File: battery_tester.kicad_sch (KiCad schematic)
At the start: 76 parts, among them J1 Conn_BAL, J10 Conn_01x02_Pin, J2 Conn_BAT, J3 Screw_Terminal_01x02, J4 Screw_Terminal_01x02, J6 CON05, J7 CON05, J8 MicroSD_Connector_500901-0801, J9 Conn_01x02_Pin, M1 OLED12864-I2C, Q1 IRF8721PBF-1, U1 STM32G484RETx, U2 ACS713xLCTR-30A, U3 BTS7004-1EPP, U4 BTS7004-1EPP, U6 TMP101, X1 ASCO

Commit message: Almost finalize schematics
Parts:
- removed J?: USB_Micro-B_Rec, _Connectors_GRZ:USB_Micro-B_Molex_105017-0001, symbol _GRZ_Connectors:USB_Micro-B_Rec
- added C29: 100nF, Capacitor_SMD:C_0603_1608Metric, symbol Device:C
- added J11: USB-C_12pin, _Connectors_GRZ:USB-C_HRO_C-31-M-12, symbol _GRZ_Connectors:USB-C_12pin
- added J5: Conn_01x02_Pin, symbol Connector:Conn_01x02_Pin
- added PB6: KSC3J, _Switches_GRZ:KSC3J, symbol _GRZ_Switches:KSC3J
- added R27, R51: 40k, Resistor_SMD:R_0603_1608Metric, symbol Device:R
- added R41, R42: 5.1K, Resistor_SMD:R_0603_1608Metric, symbol Device:R
- added TP5 (x7): TestPoint, TestPoint:TestPoint_Pad_D2.0mm, symbol Connector:TestPoint
- added X2: ASAK, _Misc_GRZ:Osc_ASAK, symbol _GRZ_Misc:ASAK
- C27, C28, C_{BYP}1, C_{OUT}1, C_{OUT}2, C_{SENSE}1, C_{SENSE}2, C_{VS}1, C_{VS}2: footprint (none) -> Capacitor_SMD:C_0603_1608Metric
- D1, D2: footprint (none) -> LED_SMD:LED_0603_1608Metric
- J10, J9: footprint (none) -> Connector_PinHeader_2.54mm:PinHeader_1x02_P2.54mm_Vertical
- J3, J4: footprint (none) -> TerminalBlock:TerminalBlock_bornier-2_P5.08mm
- J8: footprint MicroSD_500901-0801 -> _Connectors_GRZ:MicroSD_500901-0801
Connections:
- net +24V: now also J5.1 (Pin_1)
- net +3.3V: now also X1.1 (TS), C29.1, PB6.1, PB6.4, X2.1 (TS), X2.4 (VDD)
- net BOOT0: now also PB6.2, PB6.3, R51.1
- net BTS1_SENSE: now also TP5.1
- net BTS2_SENSE: now also TP5.1
- net FAN: now also R27.1
- net GND: now also C29.2, J11.A1-B12 (GND), J11.B1-A12 (GND), J11.S (Shield), J5.2 (Pin_2), R27.2, R41.2, R42.2, R51.2, X2.2 (GND)
- net SD1ck: now also TP5.1
- net SD1cs: now also TP5.1
- net SD1di: now also TP5.1
- net SD1do: now also TP5.1
- net USB_DM: now also J11.A7 (D-1), J11.B7 (D-2)
- net USB_DP: now also J11.A6 (D+1), J11.B6 (D+2)
- net USB_VBUS: now also J11.A4-B9 (VBUS), J11.B4-A9 (VBUS)
- net V_{ACS}: now also TP5.1
- net VBAT: now reaches U1.1 (VBAT)
- net LSO: now reaches U1.3 (PC14)
- net LSO: now also X2.3 (OUT)
- new net: J11.B5 (CC2), R41.1
- new net: J11.A5 (CC1), R42.1
- no-connect marks 1 -> 11
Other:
- note added: "voltage divider 5V -> 3.3V"
- note removed: "TS ? -->"
- note removed: "usb detect !!! USB-C ???"
- note removed: "voltage divider 3.3V -> 5V"
- moved on the sheet: C1, C19, C20, C21, C22, C23, C24, J6, J7

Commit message: Finish layout.
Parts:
- removed J5: Conn_01x02_Pin, symbol Connector:Conn_01x02_Pin
- removed J8: MicroSD_Connector_500901-0801, _Connectors_GRZ:MicroSD_500901-0801, symbol _GRZ_Connectors:MicroSD_Connector_500901-0801
- added H1 (x4): MountingHole, _MountingHole_GRZ:MountingHole_3.2mm_M3, symbol Mechanical:MountingHole
- added J13: MicroSD_Connector_503182-1852, _Connectors_GRZ:MicroSD_503182-1852, symbol _GRZ_Connectors:MicroSD_Connector_503182-1852
- added J5: Conn_01x07_Pin, _Connectors_GRZ:PicoBlade_53398-0771, symbol Connector:Conn_01x07_Pin
- J1: footprint Connector_JST:JST_XH_B7B-XH-A_1x07_P2.50mm_Vertical -> Connector_JST:JST_XH_S7B-XH-A_1x07_P2.50mm_Horizontal
- J10, J9: footprint Connector_PinHeader_2.54mm:PinHeader_1x02_P2.54mm_Vertical -> Connector_PinHeader_2.54mm:PinHeader_1x02_P2.54mm_Horizontal
- TP5: footprint TestPoint:TestPoint_Pad_D2.0mm -> TestPoint:TestPoint_Pad_D1.0mm
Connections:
- net +24V: now also J10.1 (Pin_1), J9.1 (Pin_1); no longer J10.2 (Pin_2), J9.2 (Pin_2)
- net +3.3V: now also J13.4 (VDD), J5.2 (Pin_2)
- net BTS1_DEN: now also U1.22 (PC4); no longer U1.20 (PA6)
- net BTS1_SENSE: now also U1.20 (PA6); no longer U1.22 (PC4)
- net BTS2_DEN: now also U1.24 (PB0); no longer U1.25 (PB1)
- net BTS2_IN: now also U1.25 (PB1); no longer U1.24 (PB0)
- net GND: now also J1.1 (Pin_1), J13.6 (GND), J13.9 (SW1), J13.S (SHIELD), J5.1 (Pin_1); no longer J1.7 (Pin_7)
- net LED_HB: now also U1.53 (PC11); no longer U1.54 (PC12)
- net LED_RUN: now also U1.52 (PC10); no longer U1.53 (PC11)
- net NFC_CLK: now also J5.6 (Pin_6)
- net NFC_IRQ: now also J5.7 (Pin_7)
- net NFC_MISO: now also J5.5 (Pin_5)
- net NFC_MOSI: now also J5.4 (Pin_4)
- net NFC_SS: now also J5.3 (Pin_3)
- net POWER_KEY: now also U1.51 (PA15); no longer U1.52 (PC10)
- net SD1ck: now also J13.5 (CLK)
- net SD1cs: now also J13.2 (CD/DAT3)
- net SD1di: now also J13.3 (CMD)
- net SD1do: now also J13.7 (DAT0)
- net at R5.1: now also J1.6 (Pin_6); no longer J1.2 (Pin_2)
- net HSE: now reaches U1.5 (PF0), X1.3 (OUT)
- net OUT1: now reaches C_{OUT}1.1, J3.1 (Pin_1), U3.10 (OUT), U3.12 (OUT), U3.13 (OUT), U3.14 (OUT), U3.8 (OUT), U3.9 (OUT)
- net at R8.1: now also J1.3 (Pin_3); no longer J1.5 (Pin_5)
- net OUT2: now reaches C_{OUT}2.1, J4.1 (Pin_1), U4.10 (OUT), U4.12 (OUT), U4.13 (OUT), U4.14 (OUT), U4.8 (OUT), U4.9 (OUT)
- net at R37.2: now also J13.8 (DAT1)
- net at Q1.5 (D), Q1.6 (D), Q1.7 (D)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: now also J10.2 (Pin_2), J9.2 (Pin_2); no longer J10.1 (Pin_1), J9.1 (Pin_1)
- net at R4.1: now also J1.7 (Pin_7); no longer J1.1 (Pin_1)
- net at R6.1: now also J1.5 (Pin_5); no longer J1.3 (Pin_3)
- net at R9.1: now also J1.2 (Pin_2); no longer J1.6 (Pin_6)
- net 24VBAT: now reaches J2.2 (Pin_2), U2.1 (IP+), U2.2 (IP+)
- net at R38.2: now also J13.1 (DAT2)
- net VBAT renamed +BATT
- new net SD_SW: J13.10 (SW2), U1.54 (PC12)
- no-connect marks 11 -> 9
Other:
- moved on the sheet: C29, J9, TP5, X2

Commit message: resistors values
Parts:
- R10, R11, R12, R13, R15, R16: value R -> 10k
- R4: value R -> 68k
- R5: value R -> 56k
- R6: value R -> 47k
- R7: value R -> 33k
- R8: value R -> 18k
- R9: value R -> 3.3k
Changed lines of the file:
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@@
       (effects (font (size 1.27 1.27)))
     )
-    (property "Value" "R" (at 355.6 52.07 90)
+    (property "Value" "56k" (at 355.6 52.07 90)
       (effects (font (size 1.27 1.27)))
     )
@@
       (effects (font (size 1.27 1.27)))
     )
-    (property "Value" "R" (at 381 74.93 0)
+    (property "Value" "10k" (at 381 74.93 0)
       (effects (font (size 1.27 1.27)))
     )
@@
       (effects (font (size 1.27 1.27)))
     )
-    (property "Value" "R" (at 368.3 74.93 0)
+    (property "Value" "10k" (at 368.3 74.93 0)
       (effects (font (size 1.27 1.27)))
     )
@@
       (effects (font (size 1.27 1.27)))
     )
-    (property "Value" "R" (at 355.6 67.31 90)
+    (property "Value" "18k" (at 355.6 67.31 90)
       (effects (font (size 1.27 1.27)))
     )
@@
       (effects (font (size 1.27 1.27)))
     )
-    (property "Value" "R" (at 355.6 46.99 90)
+    (property "Value" "68k" (at 355.6 46.99 90)
       (effects (font (size 1.27 1.27)))
     )
@@
       (effects (font (size 1.27 1.27)))
     )
-    (property "Value" "R" (at 393.7 74.93 0)
+    (property "Value" "10k" (at 393.7 74.93 0)
       (effects (font (size 1.27 1.27)))
     )
@@
       (effects (font (size 1.27 1.27)))
     )
-    (property "Value" "R" (at 387.35 74.93 0)
+    (property "Value" "10k" (at 387.35 74.93 0)
       (effects (font (size 1.27 1.27)))
     )
@@
       (effects (font (size 1.27 1.27)))
     )
-    (property "Value" "R" (at 374.65 74.93 0)
+    (property "Value" "10k" (at 374.65 74.93 0)
       (effects (font (size 1.27 1.27)))
     )
@@
       (effects (font (size 1.27 1.27)))
     )
-    (property "Value" "R" (at 355.6 62.23 90)
+    (property "Value" "33k" (at 355.6 62.23 90)
       (effects (font (size 1.27 1.27)))
     )
@@
       (effects (font (size 1.27 1.27)))
     )
-    (property "Value" "R" (at 361.95 74.93 0)
+    (property "Value" "10k" (at 361.95 74.93 0)
       (effects (font (size 1.27 1.27)))
     )
@@
       (effects (font (size 1.27 1.27)))
     )
-    (property "Value" "R" (at 355.6 72.39 90)
+    (property "Value" "3.3k" (at 355.6 72.39 90)
       (effects (font (size 1.27 1.27)))
     )
@@
       (effects (font (size 1.27 1.27)))
     )
-    (property "Value" "R" (at 355.6 57.15 90)
+    (property "Value" "47k" (at 355.6 57.15 90)
       (effects (font (size 1.27 1.27)))
     )

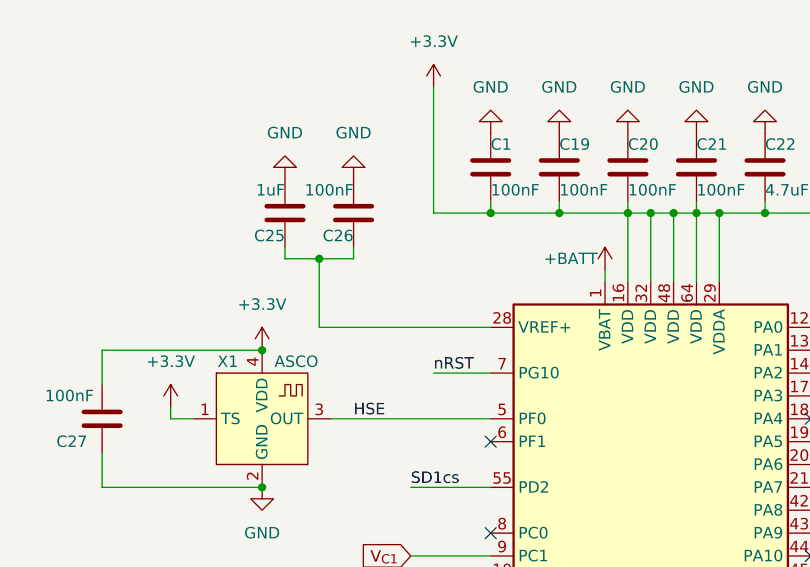
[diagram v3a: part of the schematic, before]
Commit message: Add missing VRef connection to 3V3.
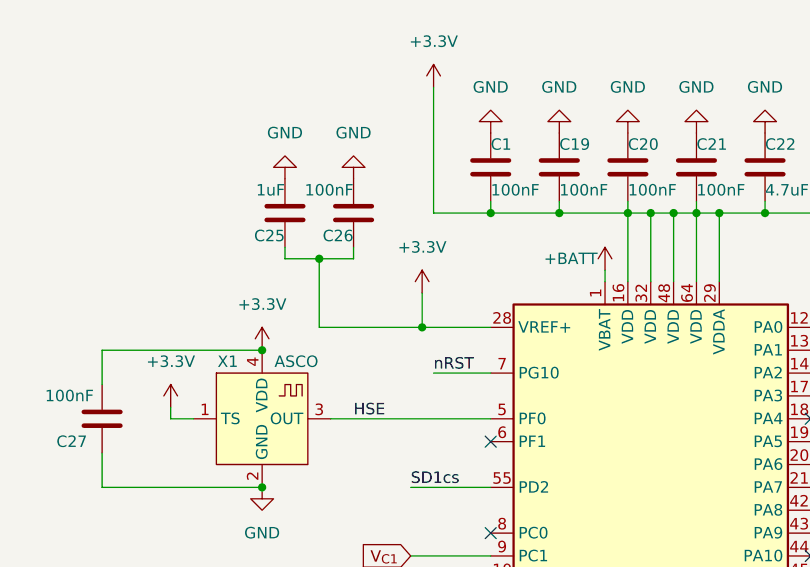
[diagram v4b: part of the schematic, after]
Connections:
- net +3.3V: now also C25.1, C26.1, U1.28 (VREF+)
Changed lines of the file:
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@@
   (junction (at 31.75 194.31) (diameter 0) (color 0 0 0 0)
+  )
+  (junction (at 173.99 121.92) (diameter 0) (color 0 0 0 0)
   )
   (junction (at 367.03 158.75) (diameter 0) (color 0 0 0 0)
@@
     (stroke (width 0) (type default))
   )
+  (wire (pts (xy 173.99 118.11) (xy 173.99 121.92))
+    (stroke (width 0) (type default))
+  )
   (wire (pts (xy 172.72 157.48) (xy 181.61 157.48))
     (stroke (width 0) (type default))
@@
   )
   (wire (pts (xy 365.76 80.01) (xy 365.76 82.55))
+    (stroke (width 0) (type default))
+  )
+  (wire (pts (xy 173.99 121.92) (xy 162.56 121.92))
     (stroke (width 0) (type default))
   )
@@
     (stroke (width 0) (type default))
   )
-  (wire (pts (xy 181.61 121.92) (xy 162.56 121.92))
+  (wire (pts (xy 181.61 121.92) (xy 173.99 121.92))
     (stroke (width 0) (type default))
   )
@@
         )
       )
+    )
+  )
+  (symbol (lib_id "power:+3.3V") (at 173.99 118.11 0) (unit 1)
+    (in_bom yes) (on_board yes) (dnp no) (fields_autoplaced)
+    (property "Reference" "#PWR0108" (at 173.99 121.92 0)
+      (effects (font (size 1.27 1.27)) hide)
+    )
+    (property "Value" "+3.3V" (at 173.99 113.03 0)
+      (effects (font (size 1.27 1.27)))
+    )
+    (property "Footprint" "" (at 173.99 118.11 0)
+      (effects (font (size 1.27 1.27)) hide)
+    )
+    (property "Datasheet" "" (at 173.99 118.11 0)
+      (effects (font (size 1.27 1.27)) hide)
+    )
+    (pin "1")
+    (instances
+      (project "battery_tester"
+        (path "/f5c3540e-6306-4c42-9ce5-3ef8f6308672"
+          (reference "#PWR0108") (unit 1)
+        )
+      )
